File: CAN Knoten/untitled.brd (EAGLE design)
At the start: 61.3 x 112.9 mm, 36 parts, among them IC1 74LS165D, IC2 74LS165D, K1 68711614522, K2 68711614522, K3 68711614522, K4 68711614522, Q1 HC49-U - 16MHz, Q2 HC49-U - xMHz

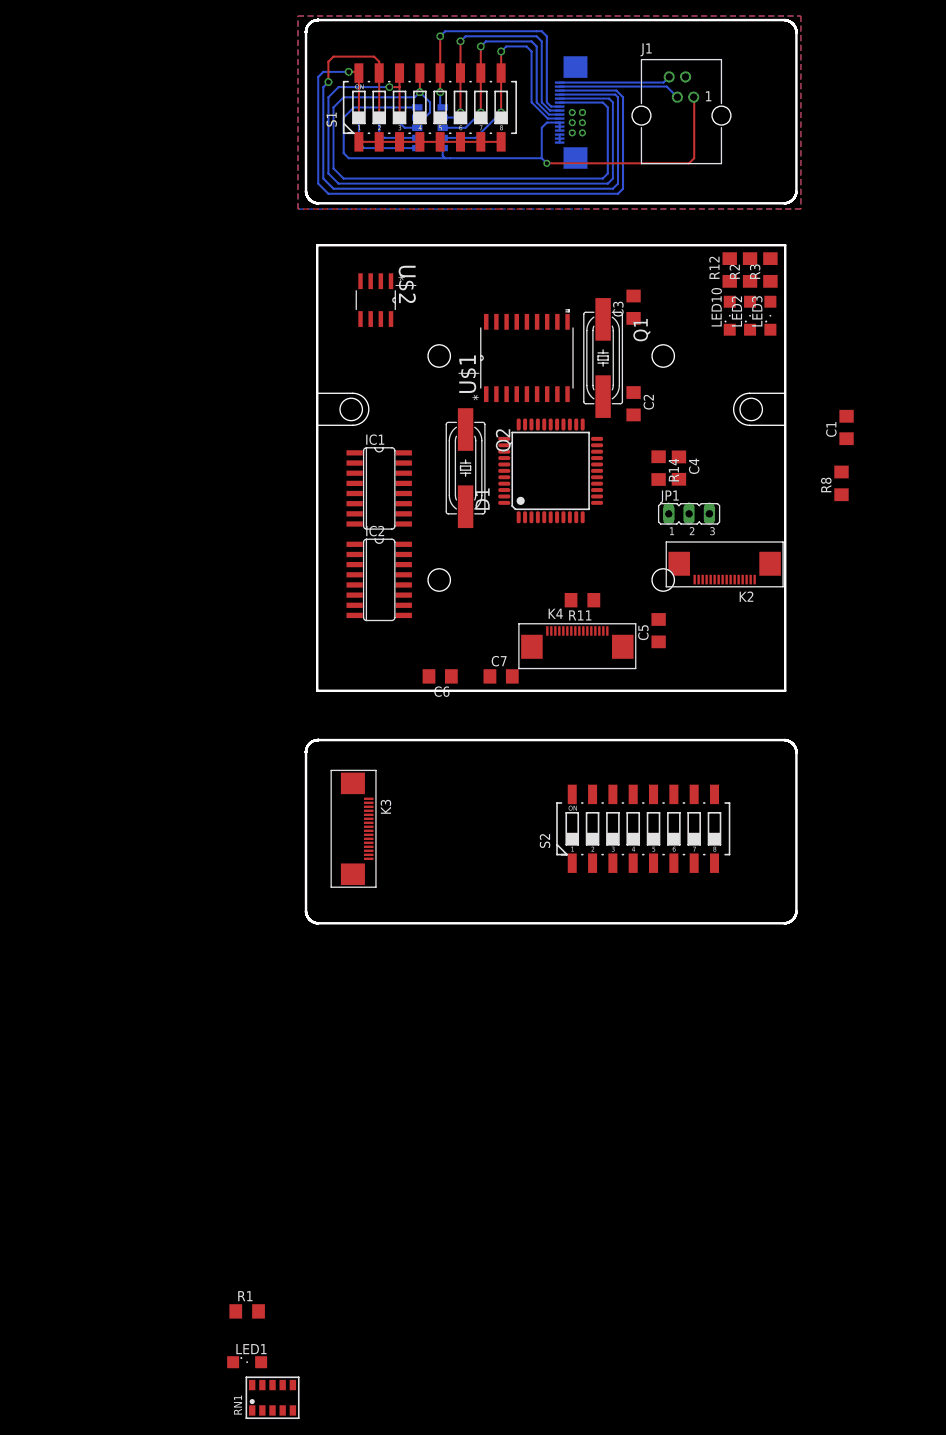
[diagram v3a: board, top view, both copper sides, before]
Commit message: 
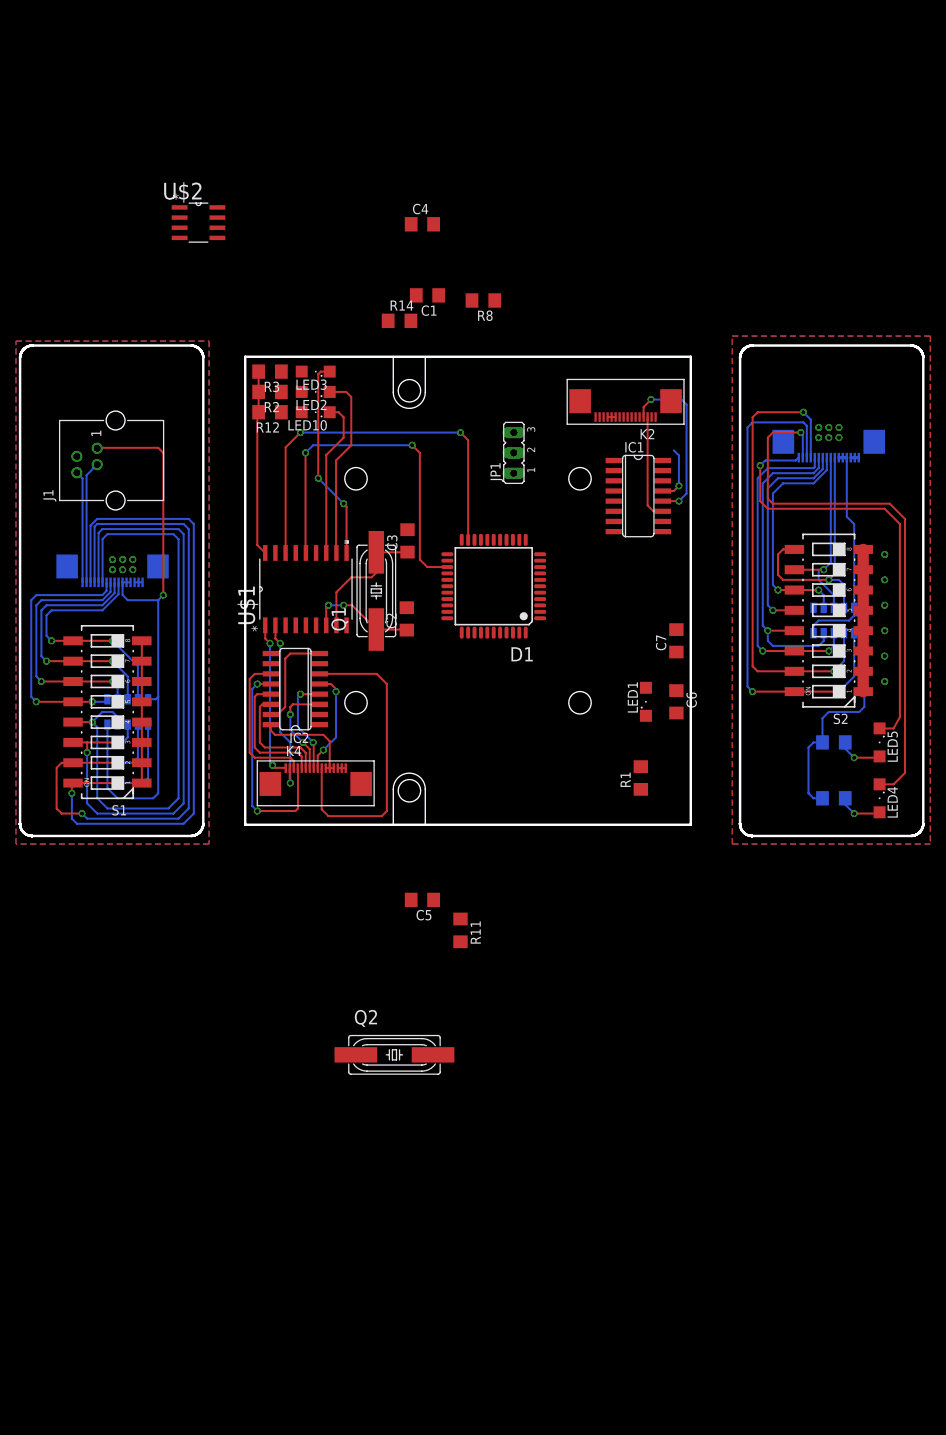
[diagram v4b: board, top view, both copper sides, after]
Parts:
- added LED4, LED5: (no value), led:SML1206
- added R4, R5: 560R, rcl:R1206
- added U$4: (no value), !!!Platinen_Logo!!!:25X25_BEST
- moved RN1 119.8 mm to (120.3, -14.6), flipped to the bottom
- moved LED1 96.4 mm to (96.8, -24.8), turned to 90 degrees
- moved S1 85.7 mm to (29.5, -26.0), turned to 90 degrees
- moved R1 82.9 mm to (96.2, -34.3), turned to 90 degrees
- moved J1 82.8 mm to (30.5, 5.39), turned to 90 degrees
- moved RN3 82.2 mm to (32.1, -26.0), turned to 0 degrees
- moved K1 81.0 mm to (30.2, -9.23), turned to 180 degrees
- moved K3 74.7 mm to (119.7, 6.35), flipped to the bottom, turned to 180 degrees
- moved Q2 73.9 mm to (65.4, -68.9), turned to 0 degrees
- moved R3 63.8 mm to (49.8, 16.5), turned to 180 degrees
- moved R2 61.9 mm to (49.8, 14.0), turned to 180 degrees
- moved R12 60.2 mm to (49.8, 11.4), turned to 180 degrees
- moved LED3 57.3 mm to (55.6, 16.5), turned to 180 degrees
- moved LED2 55.1 mm to (55.6, 14.0), turned to 180 degrees
- moved C1 54.9 mm to (69.5, 26.0), turned to 180 degrees
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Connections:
- removed net N$31: D1.21
- new net N$33: K3.1, LED5.C
- new net N$34: K3.2, LED4.C
- new net N$35: LED4.A, R4.1
- new net N$36: LED5.A, R5.1
- net MCP2515_RXCAN: now also K4.2
- net MCP2515_TXCAN: now also K4.1
- net REAR_VCC: now also R4.2, R5.2; no longer K3.1, K3.2
- net SPI_CHIP_SELECT: now also D1.21
- net VCC: no longer K4.1, K4.2
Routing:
- net N$34: track 0.00 -> 69.0 mm, vias 0 -> 1
- net N$4: track 0.00 -> 64.0 mm, vias 0 -> 2
- net N$5: track 0.00 -> 59.5 mm, vias 0 -> 2
- net REAR_VCC: track 0.00 -> 58.6 mm
- net N$33: track 0.00 -> 55.8 mm, vias 0 -> 1
- net SPI_CHIP_SELECT: track 0.00 -> 49.6 mm, vias 0 -> 2
- net SPI_MOSI: track 0.00 -> 44.8 mm, vias 0 -> 2
- net N$6: track 0.00 -> 41.5 mm, vias 0 -> 2
- net N$7: track 0.00 -> 40.8 mm, vias 0 -> 1
- net CAN_BITRATE_7: track 0.00 -> 38.7 mm
- net VCC: track 0.00 -> 37.2 mm
- net N$30: track 0.00 -> 32.1 mm, vias 0 -> 1
- net N$9: track 0.00 -> 29.4 mm, vias 0 -> 2
- net CAN_BITRATE_1: track 0.00 -> 28.4 mm, vias 0 -> 2
- net N$8: track 0.00 -> 27.5 mm, vias 0 -> 1
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- added copper zone on layer 1, net REAR_GND
- added copper zone on layer 16, net REAR_GND
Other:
- board size 61.3 x 112.9 mm -> 112.9 x 61.3 mm
- board text added: "RxD"
- board text added: "TxD"
